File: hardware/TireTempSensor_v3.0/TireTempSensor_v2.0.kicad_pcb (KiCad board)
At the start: 4 copper layers, 75 x 20.5 mm, 75 parts, among them IC2 MLX90621ESF-BAB-000-SP, IC4 TPS54202HDDCR, J2 Main connector, J3 FTSH-107-01-L-D-K, T10 TP_+5V, T14 TP_+3.3V, T15 TP_+2.6V, U1 STM32G0C1KCTxN, U2 MIC5306-2.6YD5-TR, U3 NCP715SQ33T2G, U7 ADM3057ExRW, Y1 ATX-11-F-32.000MHZ-F05-T

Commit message: Poprawione :3
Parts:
- added D7: Quad TVS, footprint:SOT95P285X140-6N, F.Cu at (154.6, 107.3)
- added D8: Quad TVS, footprint:SOT95P285X140-6N, F.Cu at (154.6, 103.6)
- C32, C33, C34, C38: footprint Capacitor_SMD:C_0603_1608Metric_Pad1.08x0.95mm_HandSolder -> Capacitor_SMD:C_0805_2012Metric_Pad1.18x1.45mm_HandSolder
- D16: footprint Diode_SMD:D_SOD-882D -> Diode_SMD:D_0603_1608Metric_Pad1.05x0.95mm_HandSolder
- moved D3 18.9 mm to (165.6, 115.3), turned to 0 degrees
- moved Y1 12.8 mm to (157.7, 90.9)
- moved C38 8.40 mm to (126.7, 97.7)
- moved FB8 8.20 mm to (126.2, 99.5)
- moved C11 8.17 mm to (155.4, 98.8), turned to -90 degrees
- moved C30 7.56 mm to (162.6, 91.6), turned to -90 degrees
- moved C39 5.92 mm to (126.2, 101.0)
- moved J3 4.44 mm to (160.7, 104.5), turned to 90 degrees
- moved C32 3.52 mm to (126.4, 106.5), turned to 0 degrees
- moved C46 3.31 mm to (128.1, 94.7)
- moved C33 2.13 mm to (126.4, 102.8)
- moved FB7 1.22 mm to (126.2, 104.6), turned to 0 degrees
- moved R6 1.06 mm to (161.8, 94.3), turned to 180 degrees
- moved FB6 0.92 mm to (110.7, 105.7)
- moved C36 0.92 mm to (110.6, 101.2)
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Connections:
- D3 pad 1: /NRST -> unconnected-(D3-CH1-Pad1)
- D3 pad 2: GND -> unconnected-(D3-GND-Pad2)
- D3 pad 3: /URAT_TX -> unconnected-(D3-CH2-Pad3)
- D3 pad 4: /URAT_RX -> unconnected-(D3-CH3-Pad4)
- D3 pad 5: /SWDIO -> unconnected-(D3-CH4-Pad5)
- D3 pad 6: /SWCLK -> unconnected-(D3-CH5-Pad6)
- D3 pad 7: /SWO -> unconnected-(D3-CH6-Pad7)
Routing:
- net /GND_ISO: track 60.5 -> 4.45 mm, vias 0 -> 9
- net +3V3: track 109.5 -> 123.2 mm, vias 7 -> 9
- net Net-(U7-VIO): track 15.1 -> 3.74 mm
- net /NRST: track 27.8 -> 35.3 mm
- net /SWO: track 4.28 -> 11.0 mm
- net GND: track 82.0 -> 75.3 mm, vias 24 -> 42
- net /SWCLK: track 21.1 -> 26.1 mm
- net /SWDIO: track 23.5 -> 28.5 mm
- net +5V: track 15.0 -> 19.1 mm
- net /OSC IN: track 20.7 -> 24.6 mm
- net /URAT_TX: track 21.5 -> 25.3 mm
- net Net-(U7-VISOIN): track 24.0 -> 25.6 mm
- net /CAN RX: track 28.0 -> 29.5 mm
- net /CAN TX: track 38.6 -> 40.0 mm
- net /CAN -: track 11.4 -> 10.2 mm
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- added copper zone on F.Cu, net /GND_ISO
- added copper zone on In1.Cu, net /GND_ISO
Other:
- board size 75 x 20.5 mm -> 75.5 x 20.5 mm

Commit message: lekkie poprawki
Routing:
- net GND: track 75.3 -> 74.5 mm, vias 42 -> 71

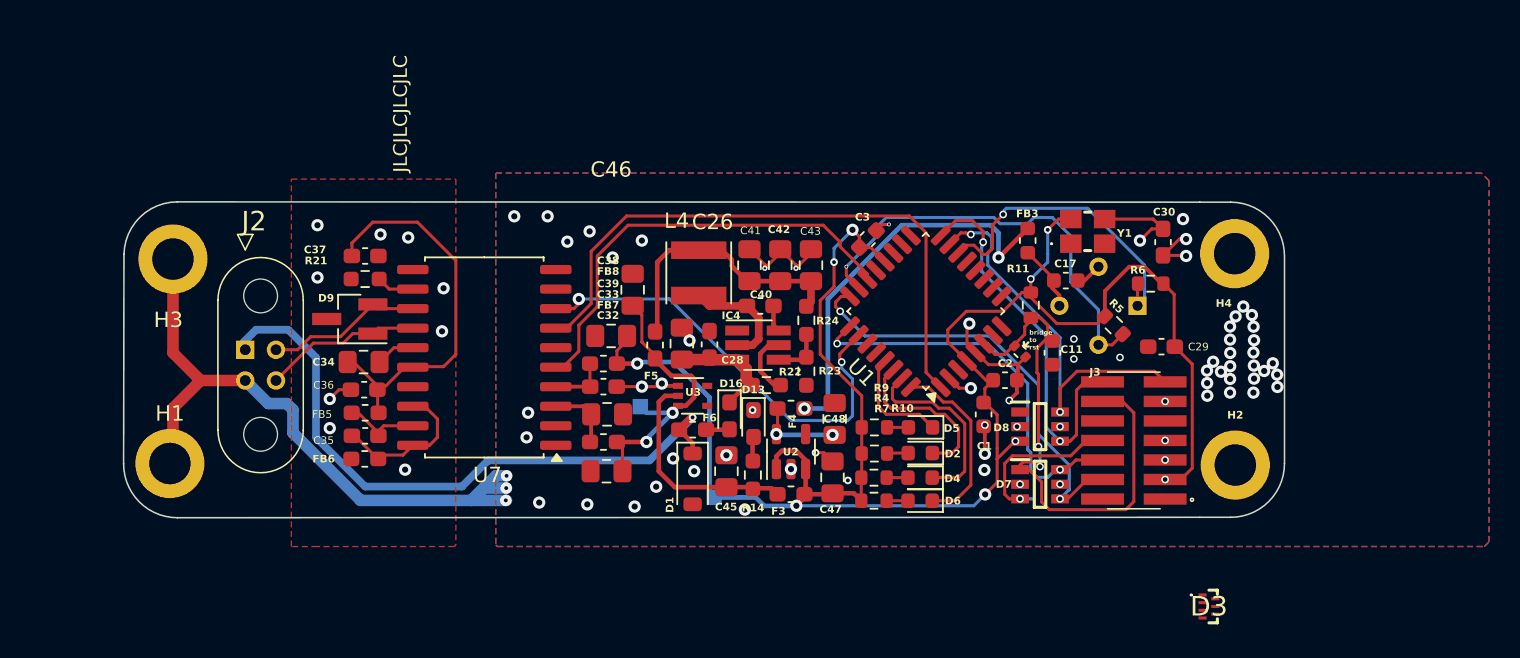
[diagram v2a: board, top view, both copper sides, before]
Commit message: Zmieniono routing w celu zmniejszenia przecięć masy
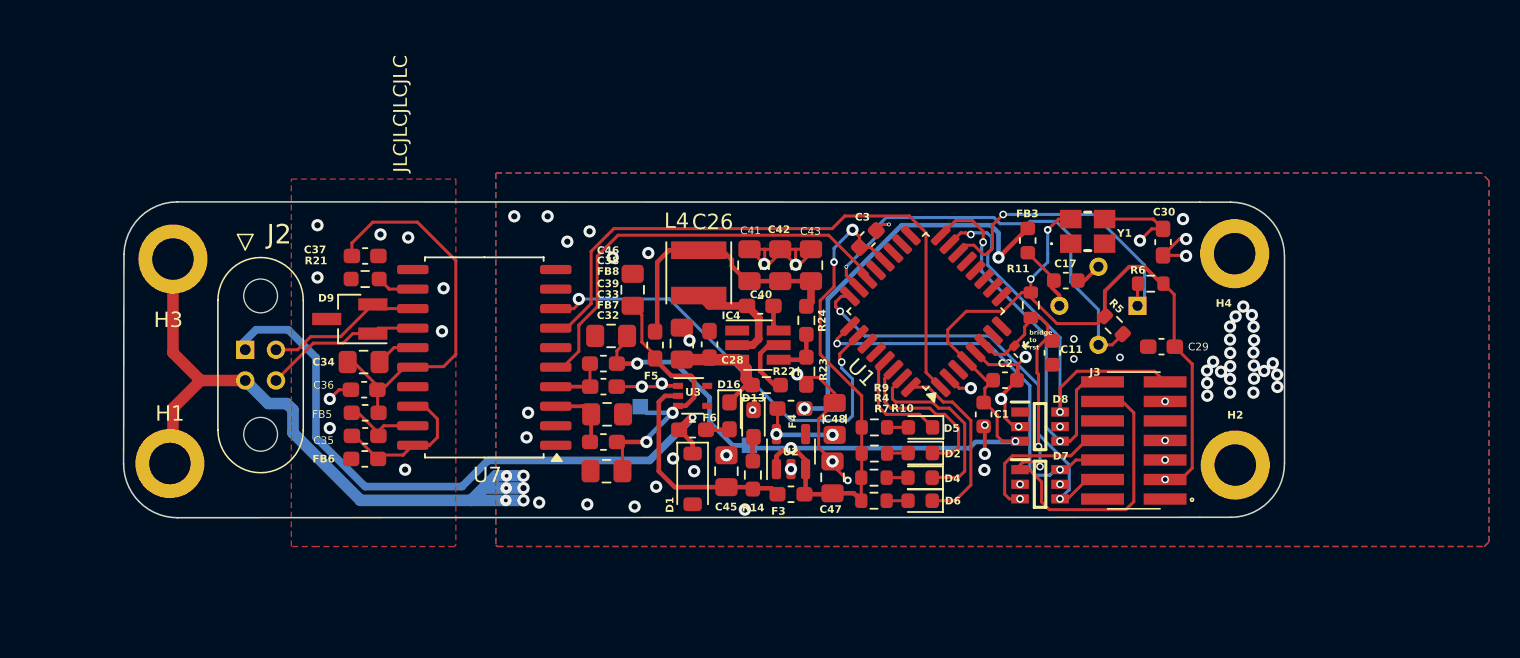
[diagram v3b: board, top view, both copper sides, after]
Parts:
- removed D3: PUSB3AB6Z, footprint:PUSB3AB6Z
- moved T14 4.09 mm to (135.7, 104.8)
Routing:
- net GND: track 74.5 -> 93.8 mm, vias 71 -> 75
- net +3V3: track 123.2 -> 115.6 mm, vias 9 -> 8
- net /SWO: track 11.0 -> 10.1 mm
- net /CAN RX: track 29.5 -> 28.8 mm

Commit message: Piotrkowe poprawy
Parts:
- added G***: LOGO, footprint:silkscreen3, F.Cu at (168.0, 99.7)
- added TP1: TestPoint_Small, TestPoint:TestPoint_Pad_D1.0mm, B.Cu at (153.3, 90.0)
- added TP2: TestPoint_Small, TestPoint:TestPoint_Pad_D1.0mm, B.Cu at (142.7, 90.9)
- added TP3: TestPoint_Small, TestPoint:TestPoint_Pad_D1.0mm, B.Cu at (148.3, 101.4)
- FB5, FB6, FB7, FB8: footprint Inductor_SMD:L_0603_1608Metric_Pad1.05x0.95mm_HandSolder -> Inductor_SMD:L_0805_2012Metric_Pad1.05x1.20mm_HandSolder
- moved C46 9.39 mm to (129.4, 104.0), turned to -90 degrees
- moved C42 8.23 mm to (129.5, 93.8), turned to -90 degrees
- moved C37 7.64 mm to (109.6, 100.1), turned to 90 degrees
- moved C36 5.58 mm to (108.6, 106.4), turned to 180 degrees
- moved F5 4.86 mm to (127.7, 93.8)
- moved C41 4.17 mm to (131.6, 93.8), turned to -90 degrees
- moved L4 4.04 mm to (136.4, 94.2)
- moved FB6 3.22 mm to (108.9, 103.0)
- moved C40 3.15 mm to (133.4, 94.8), turned to -90 degrees
- moved C39 3.03 mm to (125.8, 98.0), turned to 90 degrees
- moved FB5 2.77 mm to (108.9, 104.8), turned to 0 degrees
- moved C33 2.61 mm to (125.4, 105.2), turned to 90 degrees
- moved FB7 2.21 mm to (126.4, 102.4)
- moved C32 1.64 mm to (127.4, 105.2), turned to 90 degrees
- moved C34 1.16 mm to (111.4, 100.2), turned to -90 degrees
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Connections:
- net /CAN + renamed /CAN+
- net /CAN - renamed /CAN-
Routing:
- net Net-(U7-VISOIN): track 25.6 -> 13.9 mm
- net /Power Supply 3.3v 2.6v/BOOT_+5V: track 1.74 -> 9.51 mm, vias 0 -> 2
- net /CAN RX: track 28.8 -> 34.4 mm, vias 0 -> 2
- net /Power Supply 3.3v 2.6v/+5V_OUT: track 17.8 -> 14.7 mm
- net /STBY_CAN: track 28.7 -> 31.8 mm
- net +5V: track 19.1 -> 16.6 mm, vias 2 -> 3
- net +24V: track 42.5 -> 40.4 mm
- net /OSC IN: track 24.6 -> 26.6 mm
- net GND: track 93.8 -> 91.9 mm, vias 75 -> 39
- net /CAN TX: track 40.0 -> 41.8 mm, vias 0 -> 2
- net /SDA: track 28.4 -> 30.0 mm
- net /Power Supply 3.3v 2.6v/SW_+5V: track 7.45 -> 6.84 mm
- net Net-(C35-Pad1): track 9.96 -> 10.6 mm
- net /SWCLK: track 26.0 -> 25.4 mm
- net Net-(U7-VIO): track 3.74 -> 4.29 mm
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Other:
- board text added: "Diagnostic UART"
- board text added: "RX"
- board text added: "TX"
- board text added: "morse emited device id"

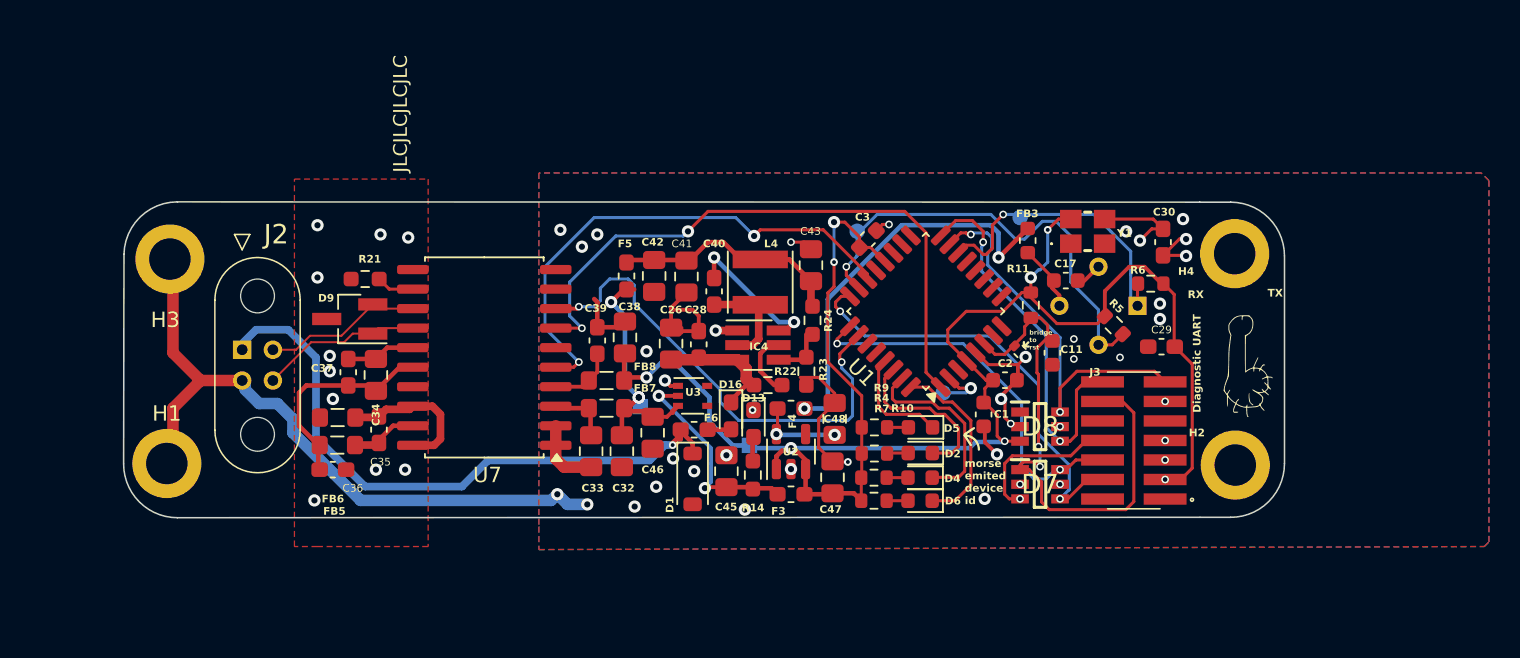
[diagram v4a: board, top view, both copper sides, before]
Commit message: updated silkscreen
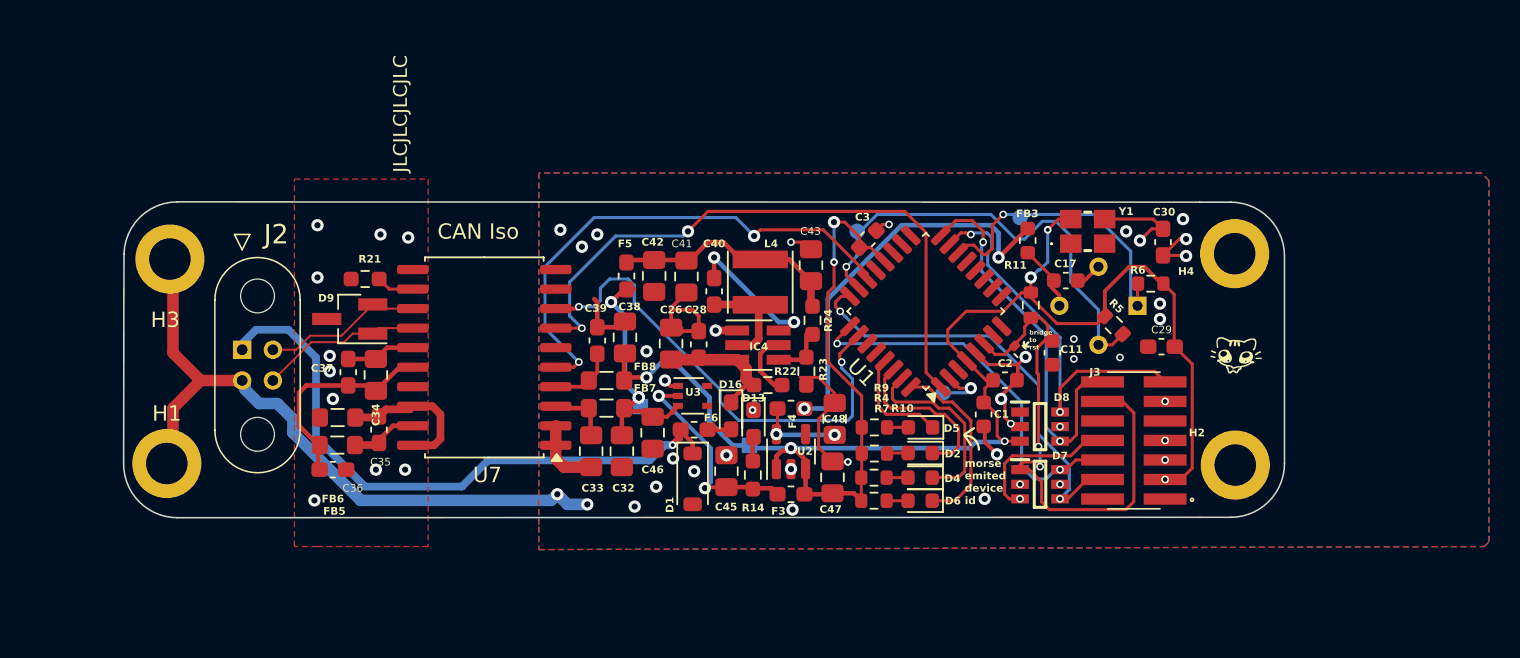
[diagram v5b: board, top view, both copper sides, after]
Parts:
- removed the G*** at (168.0, 99.7)
- added G***: LOGO, footprint:cat, F.Cu at (167.3, 98.9)
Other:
- board text added: "CAN Iso"
- board text removed: "Diagnostic UART"
- board text removed: "RX"
- board text removed: "TX"

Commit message: Z wielkim bólem przesunięte złącze aby poprawić routing cana
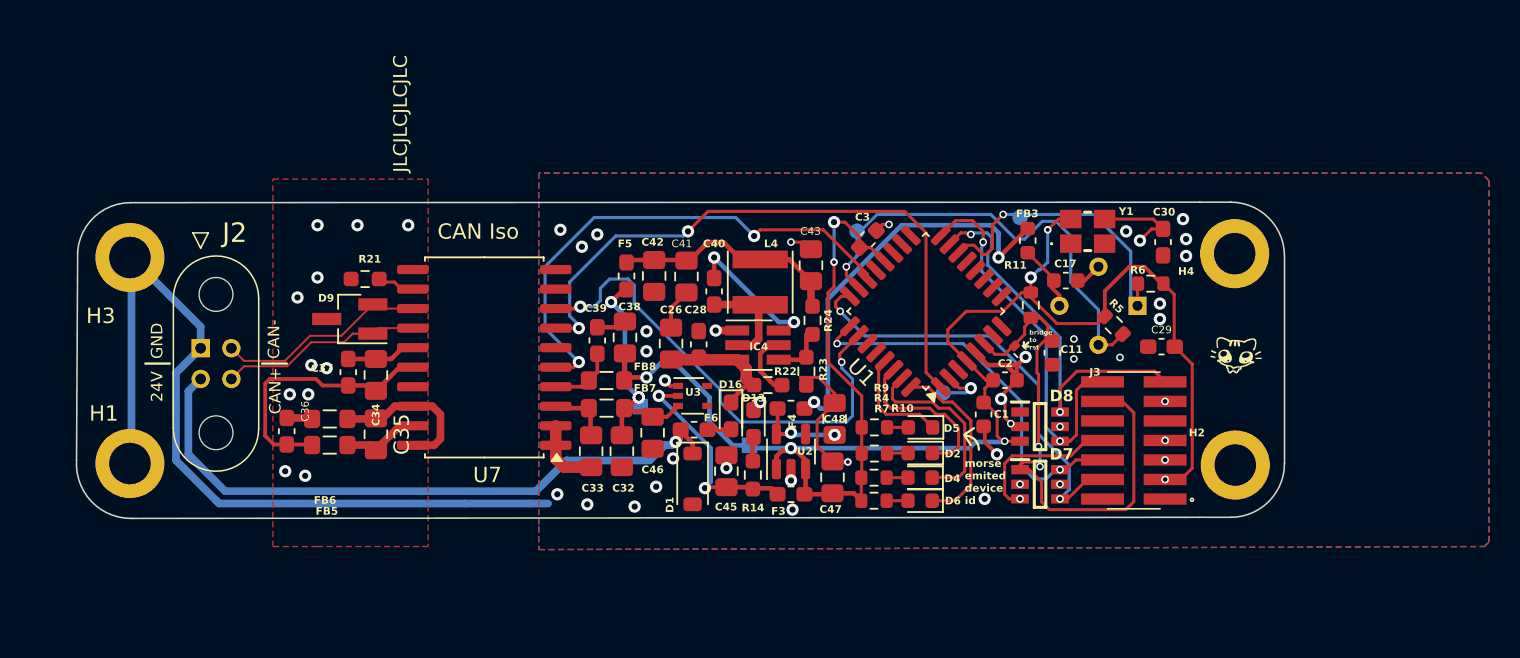
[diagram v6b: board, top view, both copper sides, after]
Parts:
- C35: footprint Capacitor_SMD:C_0603_1608Metric_Pad1.08x0.95mm_HandSolder -> Capacitor_SMD:C_0805_2012Metric_Pad1.18x1.45mm_HandSolder
- moved C36 3.91 mm to (105.6, 103.9), turned to -90 degrees
- moved J2 2.70 mm to (100.0, 98.5)
- moved H3 2.60 mm to (95.4, 92.6)
- moved H1 2.40 mm to (95.4, 106.0)
- moved FB6 0.52 mm to (108.4, 103.1)
- moved FB5 0.49 mm to (108.4, 104.8)
- moved C35 0.36 mm to (111.4, 104.1)
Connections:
- J2 pad 1: +24V -> GND
- J2 pad 2: GND -> +24V
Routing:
- net Net-(U7-VISOIN): track 13.9 -> 17.8 mm
- net /CAN-: track 10.4 -> 13.8 mm
- net GND: track 91.9 -> 94.6 mm
- net /CAN+: track 10.5 -> 13.2 mm
- net /GND_ISO: track 4.50 -> 6.08 mm, vias 10 -> 11
- net +24V: track 40.4 -> 41.8 mm
- net Net-(U7-VISOOUT): track 4.29 -> 5.20 mm
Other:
- board size 75.5 x 20.5 mm -> 78.6 x 20.6 mm
- board text added: "CAN+"
- board text added: "CAN-"

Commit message: Added aditional emi prevention measures
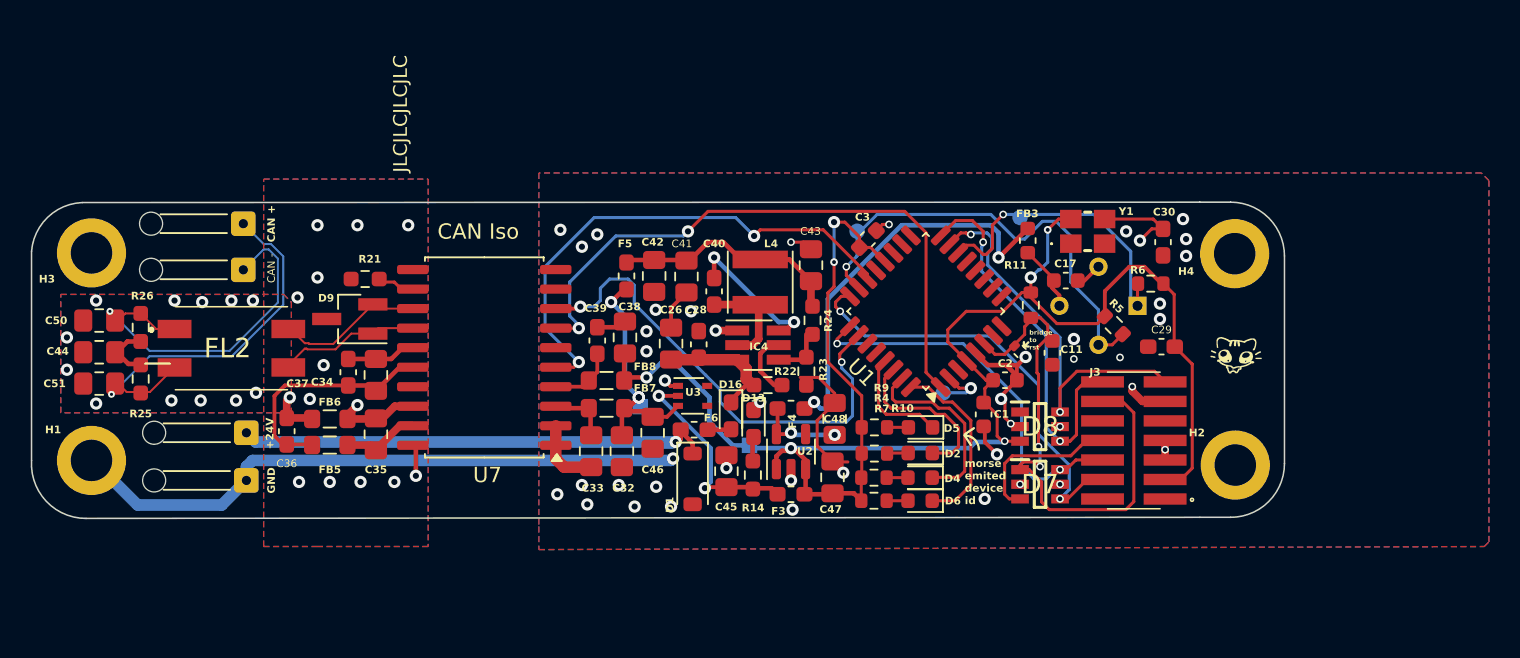
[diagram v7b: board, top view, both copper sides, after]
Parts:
- removed J2: Main connector, footprint:M80-51004YY
- added +24V: Conn_01x01, Connector_Wire:SolderWire-0.1sqmm_1x01_D0.4mm_OD1mm_Relief, F.Cu at (103.0, 104.0)
- added C44: 4.7n, Capacitor_SMD:C_0805_2012Metric_Pad1.18x1.45mm_HandSolder, F.Cu at (93.4, 98.8)
- added C50: 50p X7R, Capacitor_SMD:C_0805_2012Metric_Pad1.18x1.45mm_HandSolder, F.Cu at (93.4, 96.7)
- added C51: 50p X7R, Capacitor_SMD:C_0805_2012Metric_Pad1.18x1.45mm_HandSolder, F.Cu at (93.4, 100.8)
- added CAN +: Conn_01x01, Connector_Wire:SolderWire-0.1sqmm_1x01_D0.4mm_OD1mm_Relief, F.Cu at (102.8, 90.4)
- added CAN -: Conn_01x01, Connector_Wire:SolderWire-0.1sqmm_1x01_D0.4mm_OD1mm_Relief, F.Cu at (102.8, 93.4)
- added FL2: Common mode choke, footprint:DR331513BE, F.Cu at (101.8, 98.5)
- added GND: Conn_01x01, Connector_Wire:SolderWire-0.1sqmm_1x01_D0.4mm_OD1mm_Relief, F.Cu at (103.0, 107.1)
- added R25: 60R, Resistor_SMD:R_0603_1608Metric_Pad0.98x0.95mm_HandSolder, F.Cu at (96.1, 100.5)
- added R26: 60R, Resistor_SMD:R_0603_1608Metric_Pad0.98x0.95mm_HandSolder, F.Cu at (96.1, 97.2)
- moved H3 2.52 mm to (92.9, 92.3)
- moved H1 2.51 mm to (92.9, 105.8)
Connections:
- net /CAN+ renamed /CAN/CAN_internal+
- net /CAN- renamed /CAN/CAN_internal-
- H3 pad 1: GND -> unconnected-(H3-Pad1)
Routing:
- net /CAN+: track 0.00 -> 25.8 mm, vias 0 -> 1
- net /CAN-: track 0.00 -> 24.5 mm, vias 0 -> 1
- net GND: track 94.6 -> 82.6 mm, vias 39 -> 43
- net +24V: track 41.8 -> 31.5 mm
- net /CAN/CAN_internal-: track 13.8 -> 9.36 mm
- net /CAN/CAN_internal+: track 13.2 -> 9.14 mm
- net Net-(C44-Pad1): track 0.00 -> 3.73 mm
- net Net-(U7-VISOIN): track 17.8 -> 14.1 mm
- net +3V3: track 115.1 -> 112.5 mm, vias 8 -> 7
- net Net-(C35-Pad1): track 10.9 -> 13.4 mm, vias 0 -> 2
- net +5V: track 16.2 -> 14.4 mm
- net /NRST: track 35.3 -> 33.5 mm
- net /Power Supply 3.3v 2.6v/+5V_OUT: track 14.7 -> 13.1 mm
- net /SCL: track 20.3 -> 19.0 mm
- net /URAT_TX: track 25.3 -> 24.0 mm
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- added copper zone on B.Cu, net /GND_ISO
- added copper zone on In2.Cu, net /GND_ISO
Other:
- board size 78.6 x 20.6 mm -> 81.5 x 20.6 mm
- board text removed: "CAN+"
- board text removed: "CAN-"
